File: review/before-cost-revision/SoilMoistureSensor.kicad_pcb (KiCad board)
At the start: 2 copper layers, 55 x 198.5 mm, 55 parts, among them J1 Conn_01x02, J2 Conn_01x04, J3 Conn_01x02, J4 PCB capacitive probe, Q1 AO3401A, SW1 TS-1088-AR02016, SW2 TS-1088-AR02016, U1 BQ25570, U2 ESP32-C3-WROOM-02-N4, U3 TLC555CDR, U4 TPS62842DGRR

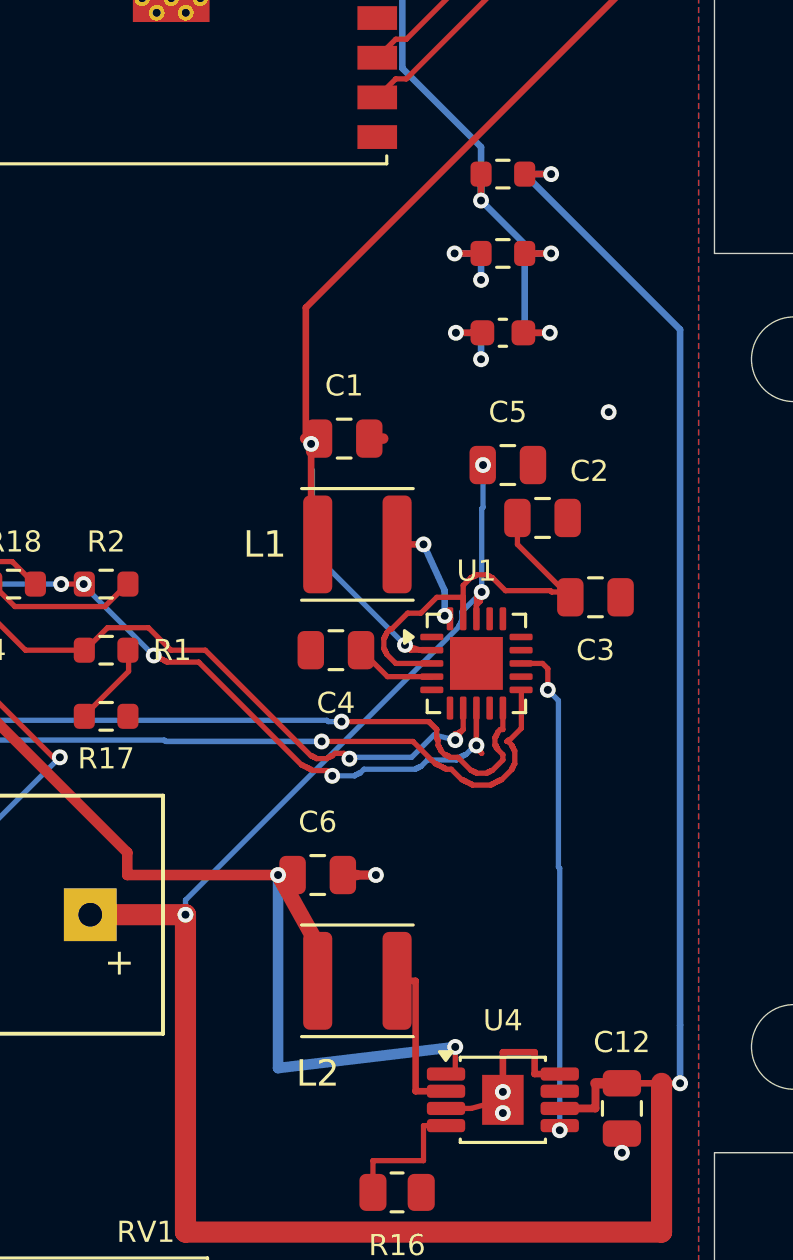
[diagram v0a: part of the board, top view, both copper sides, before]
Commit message: reworked some parts to get jlcpcb basic, reworked inductors
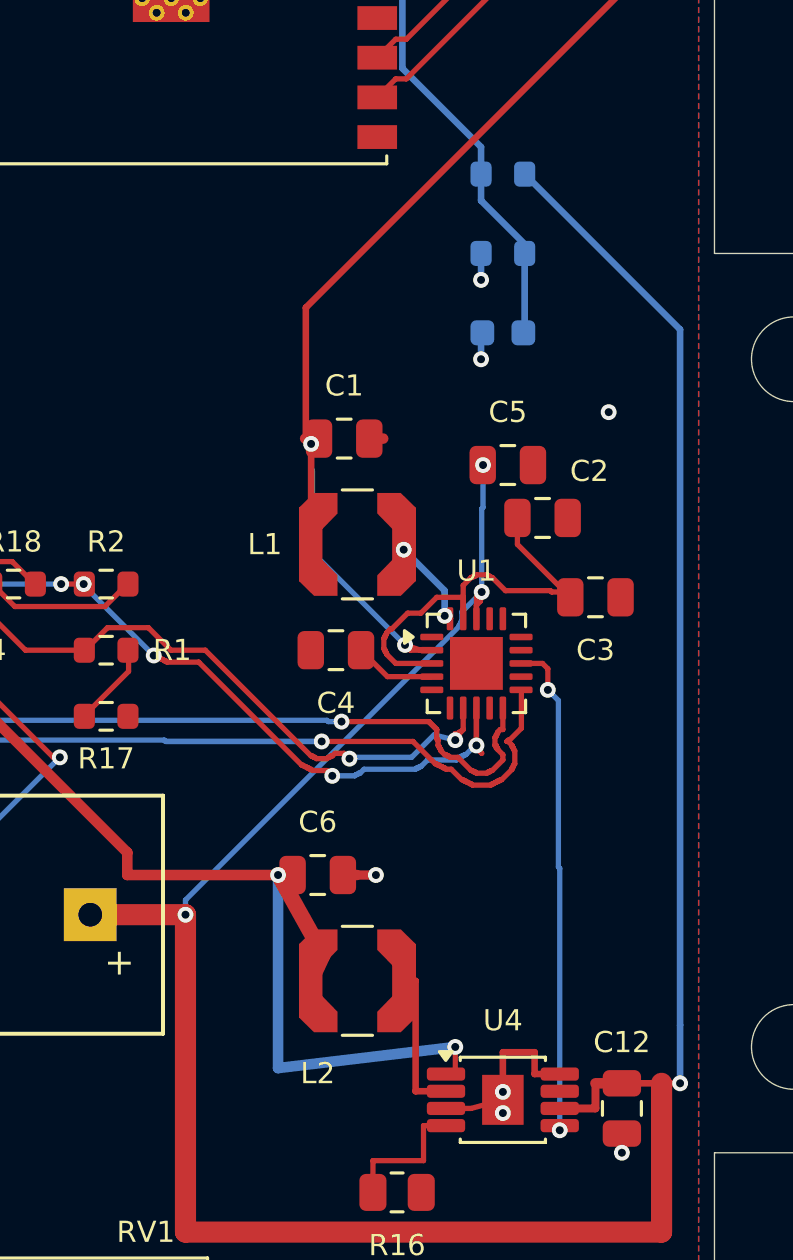
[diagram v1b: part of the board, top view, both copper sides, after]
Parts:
- C13, R25: moved to B.Cu
- L1, L2: footprint Inductor_SMD:L_Changjiang_FNR4018S -> Inductor_SMD:L_Coilcraft_LPS4018
- R24: value 2M 1% -> 2.2M 1%; moved to B.Cu
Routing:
- net /VCAP_ADC: track 23.8 -> 17.8 mm, vias 4 -> 1
- net /GND: track 37.0 -> 33.0 mm, vias 19 -> 17
- net /VBAT: track 107.4 -> 105.4 mm, vias 5 -> 4
- net /LBOOST: track 4.13 -> 3.61 mm
